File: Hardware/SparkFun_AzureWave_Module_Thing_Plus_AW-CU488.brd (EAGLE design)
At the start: 22.9 x 77.5 mm, 113 parts, among them J1 THING_PLUS, J3 QWIIC_RA, J5 USB-C, Q1 2.5A/30V, Q2 MBT3904DW1T1, U2 CP210X, U3 AP2112, U4 MCP73831

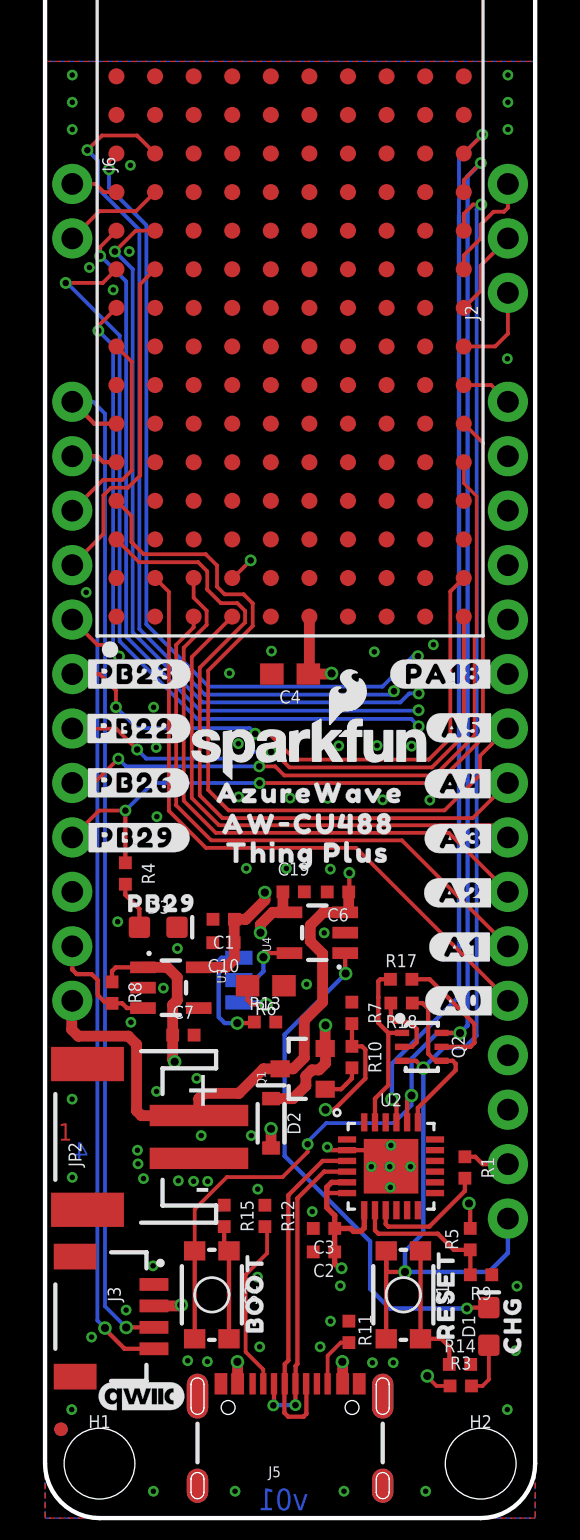
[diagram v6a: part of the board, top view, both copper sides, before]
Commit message: pre-design review notes and fixes
-power symbols, Q1, U3, U4 updated to latest libraries
-consolidated all low current signals to 10mils vias. V_USB (x4), 3.3V (x3), VIN (x2)  are still 15mil for higher current capabilities.
-Center anchor for section text in sch
-added via near transitioning digital signals near PB26/PB28 PTH headers
-moved R15 about 20mil to the right to give more room for rework/give more room for the JST connector
-reduced paste on modules pads by 2mils on either side (for a reduction total on the diameter of the paste hole of 4 mils).
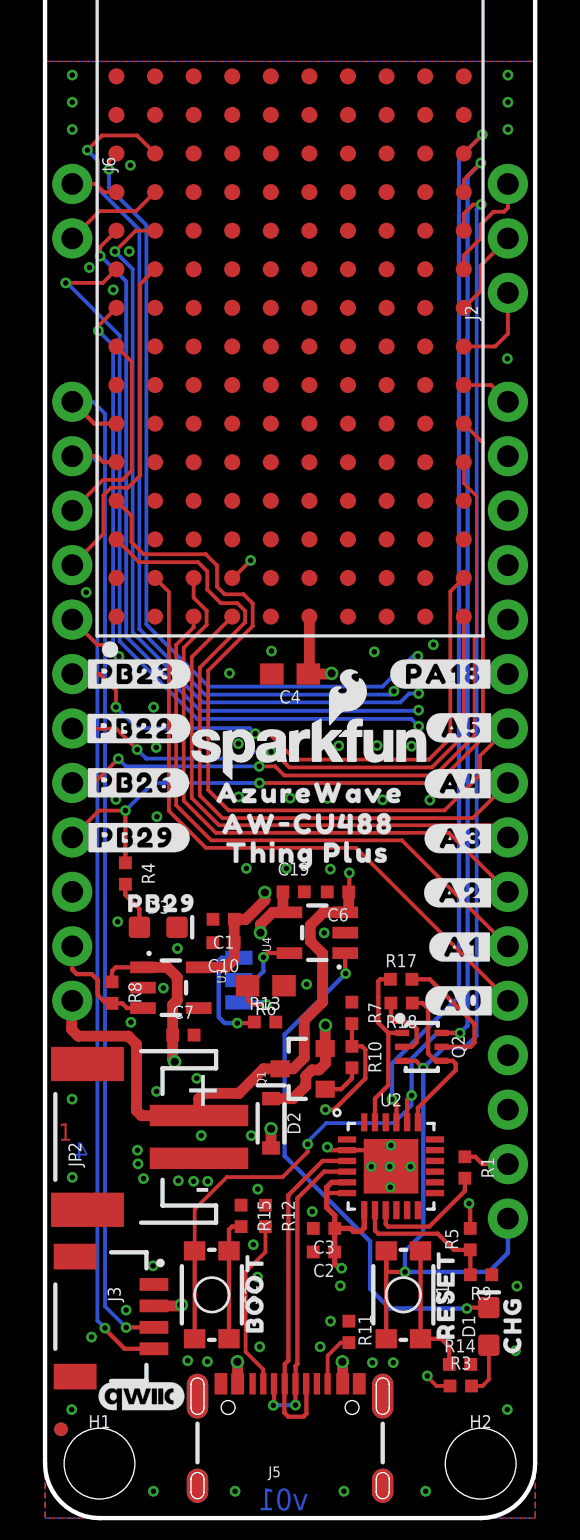
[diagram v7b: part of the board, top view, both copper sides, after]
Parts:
- Q1: value 2.5A/30V -> 3.1A/30V/105mΩ; device SparkFun-DiscreteSemi:SOT23-3@1 -> SparkFun-DiscreteSemi:SOT23-3
- R6: device SparkFun-Resistors:0603@1 -> SparkFun-Resistors:0603
- U3: value AP2112 -> AP2112K-3.3V; device SparkFun-PowerIC:SOT23-5 -> SparkFun-IC-Power:SOT23-5
- U4: device SparkFun-PowerIC:SOT23-5 -> SparkFun-IC-Power:SOT23-5
- moved R15 0.79 mm to (9.14, 14.1)
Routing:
- net GND: vias 77 -> 79

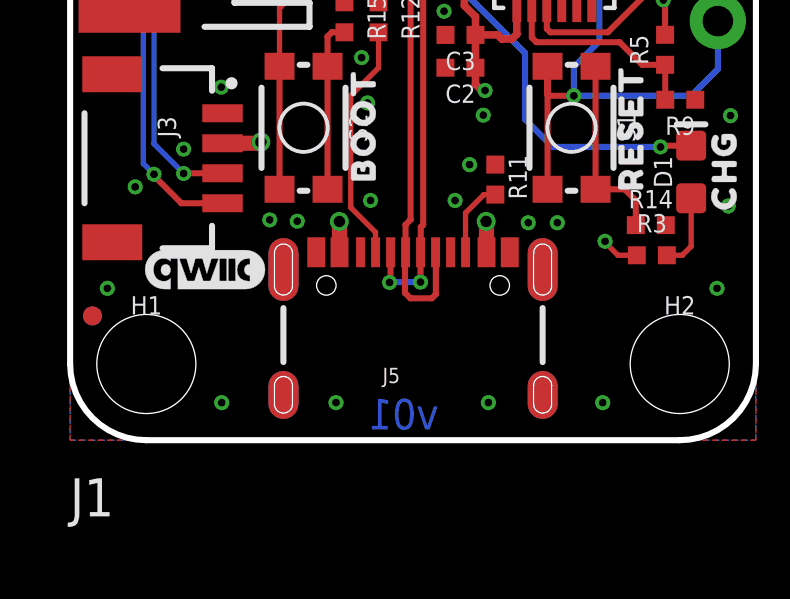
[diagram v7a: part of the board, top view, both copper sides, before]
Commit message: added USB Shield GND jumper
-added "shield" net polygons (and via)  to connect all 8 shield pads. And add a little extra strength.
-added jumper to connect USB-C shield to GND (normally closed via trace).
-moved OSHW logo and version text.
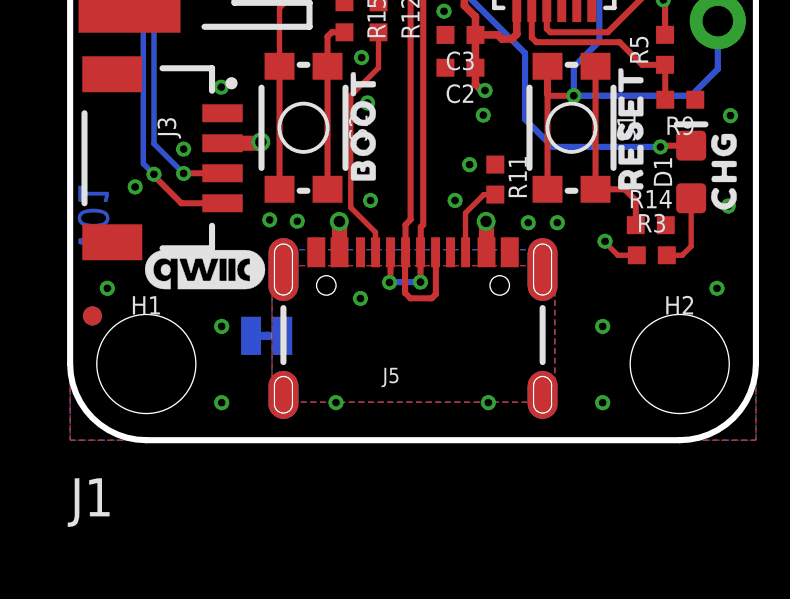
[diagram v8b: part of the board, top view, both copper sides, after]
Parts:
- added U$20: (no value), output:#USBSHLD#GND#3
- added USBSHLD: (no value), SparkFun-Jumpers:SMT-JUMPER_2_NC_TRACE_SILK
- moved LOGO2 55.9 mm to (11.4, 59.7)
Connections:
- new net USB_SHLD: J5.SHLD1, J5.SHLD2, J5.SHLD3, J5.SHLD4, J5.SHLD5, J5.SHLD6, J5.SHLD7, J5.SHLD8, USBSHLD.2
- net GND: now also USBSHLD.1
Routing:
- net GND: vias 79 -> 81
- added copper zone on layer 1, net USB_SHLD
- added copper zone on layer 16, net USB_SHLD
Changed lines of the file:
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@@
 <wire x1="2.54" y1="0" x2="20.32" y2="0" width="0.2032" layer="20"/>
 <wire x1="20.32" y1="0" x2="22.86" y2="2.54" width="0.2032" layer="20" curve="90"/>
-<text x="12.2809" y="0.868678125" size="1.016" layer="16" font="vector" ratio="20" rot="MR0" align="center-left">v01</text>
+<text x="0.782321875" y="8.5979" size="1.016" layer="16" font="vector" ratio="20" rot="MR270" align="center-left">v01</text>
 <text x="0.6223" y="17.604740625" size="0.8128" layer="1" font="vector" ratio="25">1</text>
 <text x="1.3843" y="17.604740625" size="0.8128" layer="2" font="vector" ratio="25">2</text>
@@
 <attribute name="VALUE" x="11.577315625" y="29.6926" size="0.6096" layer="27" font="vector" ratio="20" rot="R180" align="top-center"/>
 </element>
-<element name="LOGO2" library="SparkFun-Aesthetics" package="OSHW-LOGO-MINI" value="OSHW-LOGOMINI" x="11.43" y="3.81" smashed="yes" rot="MR0"/>
+<element name="LOGO2" library="SparkFun-Aesthetics" package="OSHW-LOGO-MINI" value="OSHW-LOGOMINI" x="11.43" y="59.69" smashed="yes" rot="MR0"/>
 <element name="J3" library="SparkFun-Connectors" package="JST04_1MM_RA" value="QWIIC_RA" x="5.08" y="9.398" smashed="yes" rot="R270">
 <attribute name="NAME" x="2.921" y="10.795" size="0.6096" layer="25" font="vector" ratio="20" rot="R270"/>
@@
 <element name="LOGO5" library="SparkFun-Aesthetics" package="SFE_LOGO_NAME_FLAME_.1" value="SFE_LOGO_NAME_FLAME.1_INCH" x="12.38758125" y="35.892740625" smashed="yes"/>
 <element name="U$18" library="output" package="#A0#30" value="" x="19.453859375" y="24.127459375" smashed="yes"/>
+<element name="USBSHLD" library="SparkFun-Jumpers" package="SMT-JUMPER_2_NC_TRACE_SILK" package3d_urn="urn:adsk.eagle:package:39281/1" value="" x="6.5532" y="3.4798" smashed="yes" rot="MR180">
+<attribute name="NAME" x="6.5532" y="2.3368" size="0.6096" layer="26" font="vector" ratio="20" rot="MR180" align="bottom-center"/>
+<attribute name="VALUE" x="6.5532" y="4.6228" size="0.6096" layer="28" font="vector" ratio="20" rot="MR180" align="top-center"/>
+</element>
+<element name="U$20" library="output" package="#USBSHLD#GND#3" value="" x="12.573" y="3.429" smashed="yes" rot="MR0"/>
 </elements>
 <signals>
@@
 <contactref element="C2" pad="2"/>
 <contactref element="C3" pad="2"/>
-<polygon width="0.2032" layer="1" isolate="0.1778">
+<polygon width="0.2032" layer="1" isolate="0.1778" rank="2">
 <vertex x="0" y="0"/>
 <vertex x="0" y="67.945"/>
@@
 <vertex x="22.86" y="0"/>
 </polygon>
-<polygon width="0.2032" layer="16" isolate="0.1778">
+<polygon width="0.2032" layer="16" isolate="0.1778" rank="2">
 <vertex x="0" y="0"/>
 <vertex x="22.86" y="0"/>
@@
 <via x="3.304553125" y="33.522909375" extent="1-16" drill="0.254"/>
 <via x="9.715503125" y="12.7533375" extent="1-16" drill="0.254"/>
+<contactref element="USBSHLD" pad="1"/>
+<via x="5.052059375" y="3.79221875" extent="1-16" drill="0.254"/>
+<via x="17.752059375" y="3.79221875" extent="1-16" drill="0.254"/>
 </signal>
 <signal name="V_USB">
@@
 <wire x1="20.81" y1="52.85" x2="21.59" y2="52.07" width="0.1778" layer="1"/>
 </signal>
+<signal name="USB_SHLD">
+<contactref element="J5" pad="SHLD6"/>
+<contactref element="J5" pad="SHLD7"/>
+<contactref element="J5" pad="SHLD8"/>
+<contactref element="J5" pad="SHLD4"/>
+<contactref element="J5" pad="SHLD5"/>
+<contactref element="J5" pad="SHLD3"/>
+<contactref element="J5" pad="SHLD1"/>
+<contactref element="J5" pad="SHLD2"/>
+<contactref element="USBSHLD" pad="2"/>
+<polygon width="0.2032" layer="1" isolate="0.254">
+<vertex x="16.1544" y="5.8166"/>
+<vertex x="6.731" y="5.8166"/>
+<vertex x="6.731" y="1.27"/>
+<vertex x="16.1544" y="1.27"/>
+</polygon>
+<polygon width="0.2032" layer="16" isolate="0.254">
+<vertex x="6.731" y="1.27"/>
+<vertex x="16.1544" y="1.27"/>
+<vertex x="16.1544" y="6.35"/>
+<vertex x="6.731" y="6.35"/>
+</polygon>
+<via x="9.6774" y="4.7244" extent="1-16" drill="0.254"/>
+</signal>
 </signals>
